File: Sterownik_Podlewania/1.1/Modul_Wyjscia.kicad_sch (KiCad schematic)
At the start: 2 parts, among them J9 Screw_Terminal_01x02, U2 HHG1D-1

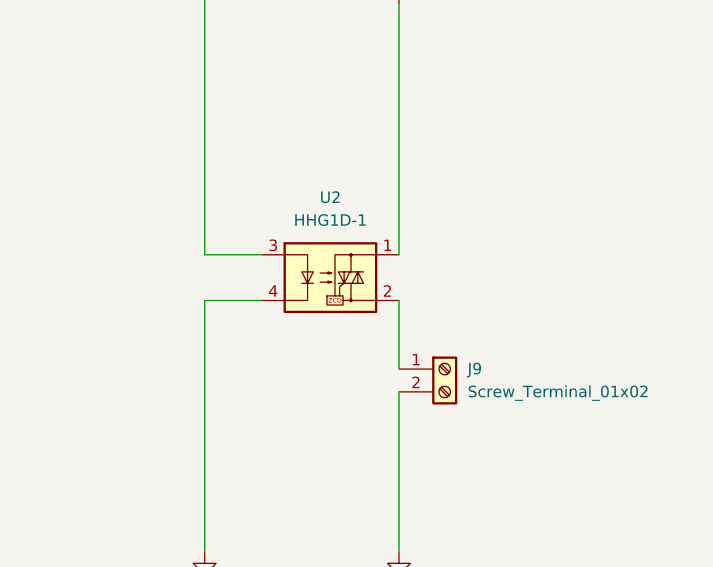
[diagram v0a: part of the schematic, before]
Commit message: Poprawiono błędy połączeń SDA,SCL, dodno drugą magistralę I2C, pociągnięcie nowych ścieżek
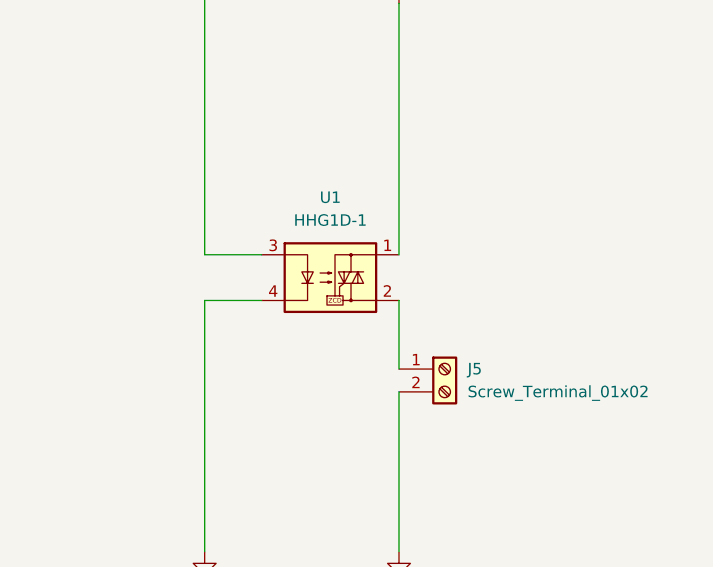
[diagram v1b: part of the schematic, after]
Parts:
- renumbered J9 to J5, U2 to U1
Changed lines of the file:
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@@
 		(dnp no)
 		(fields_autoplaced yes)
-		(property "Reference" "J9"
+		(property "Reference" "J5"
 			(at 127 119.3799 0)
 			(effects
@@
 			(project "Sterownik_Podlewania"
 				(path "/a66bdf1f-0e2a-4cc5-beb1-605f2a3b9885/35770c0e-1214-4968-b3c8-676b712c9d6d"
-					(reference "J10")
+					(reference "J6")
 					(unit 1)
 				)
 				(path "/a66bdf1f-0e2a-4cc5-beb1-605f2a3b9885/6e956094-fc15-4c8c-a9c0-3072cf96750e"
+					(reference "J5")
+					(unit 1)
+				)
+				(path "/a66bdf1f-0e2a-4cc5-beb1-605f2a3b9885/76d9d54a-15a3-400e-aaa0-0af773ab885c"
+					(reference "J8")
+					(unit 1)
+				)
+				(path "/a66bdf1f-0e2a-4cc5-beb1-605f2a3b9885/995f053e-6bfd-4935-9460-d34c9e8248bd"
 					(reference "J9")
 					(unit 1)
 				)
-				(path "/a66bdf1f-0e2a-4cc5-beb1-605f2a3b9885/76d9d54a-15a3-400e-aaa0-0af773ab885c"
-					(reference "J12")
-					(unit 1)
-				)
-				(path "/a66bdf1f-0e2a-4cc5-beb1-605f2a3b9885/995f053e-6bfd-4935-9460-d34c9e8248bd"
-					(reference "J13")
-					(unit 1)
-				)
 				(path "/a66bdf1f-0e2a-4cc5-beb1-605f2a3b9885/aaafd38c-ffc0-4fc7-936b-5b26ec62426f"
-					(reference "J11")
+					(reference "J7")
 					(unit 1)
 				)
@@
 		(dnp no)
 		(fields_autoplaced yes)
-		(property "Reference" "U2"
+		(property "Reference" "U1"
 			(at 111.76 100.33 0)
 			(effects
@@
 			(project ""
 				(path "/a66bdf1f-0e2a-4cc5-beb1-605f2a3b9885/35770c0e-1214-4968-b3c8-676b712c9d6d"
-					(reference "U7")
+					(reference "U2")
 					(unit 1)
 				)
 				(path "/a66bdf1f-0e2a-4cc5-beb1-605f2a3b9885/6e956094-fc15-4c8c-a9c0-3072cf96750e"
-					(reference "U2")
+					(reference "U1")
 					(unit 1)
 				)
 				(path "/a66bdf1f-0e2a-4cc5-beb1-605f2a3b9885/76d9d54a-15a3-400e-aaa0-0af773ab885c"
-					(reference "U9")
+					(reference "U3")
 					(unit 1)
 				)
 				(path "/a66bdf1f-0e2a-4cc5-beb1-605f2a3b9885/995f053e-6bfd-4935-9460-d34c9e8248bd"
-					(reference "U10")
+					(reference "U6")
 					(unit 1)
 				)
 				(path "/a66bdf1f-0e2a-4cc5-beb1-605f2a3b9885/aaafd38c-ffc0-4fc7-936b-5b26ec62426f"
-					(reference "U8")
-					(unit 1)
-				)
+					(reference "U4")
+					(unit 1)
+				)

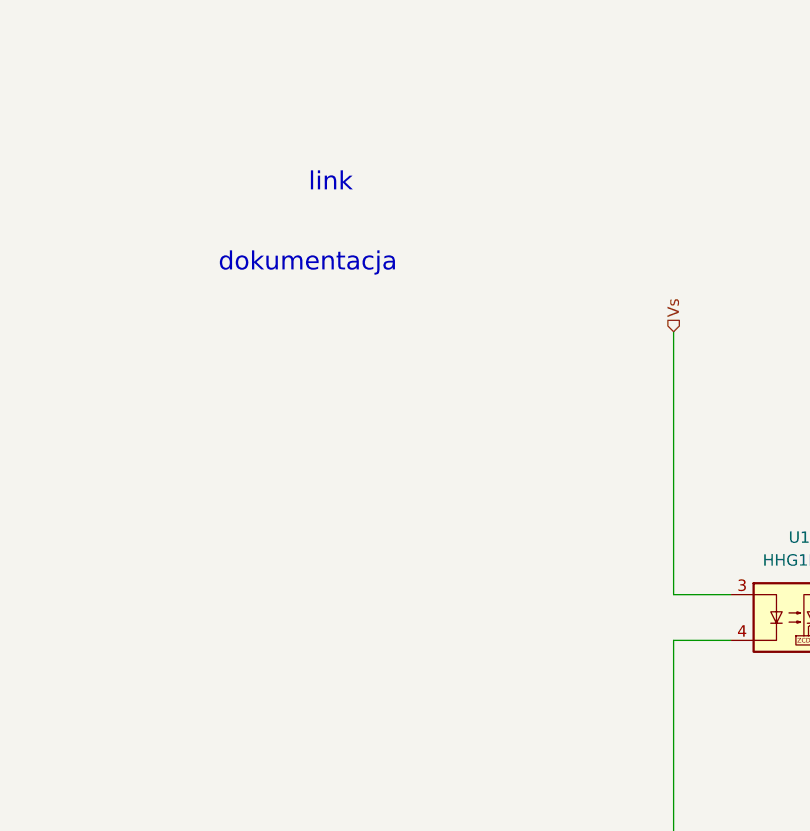
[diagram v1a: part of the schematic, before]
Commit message: Poprawki schematu modułu zaworu, usunięcie przekaźnika, przygotowanie schematu zasilania
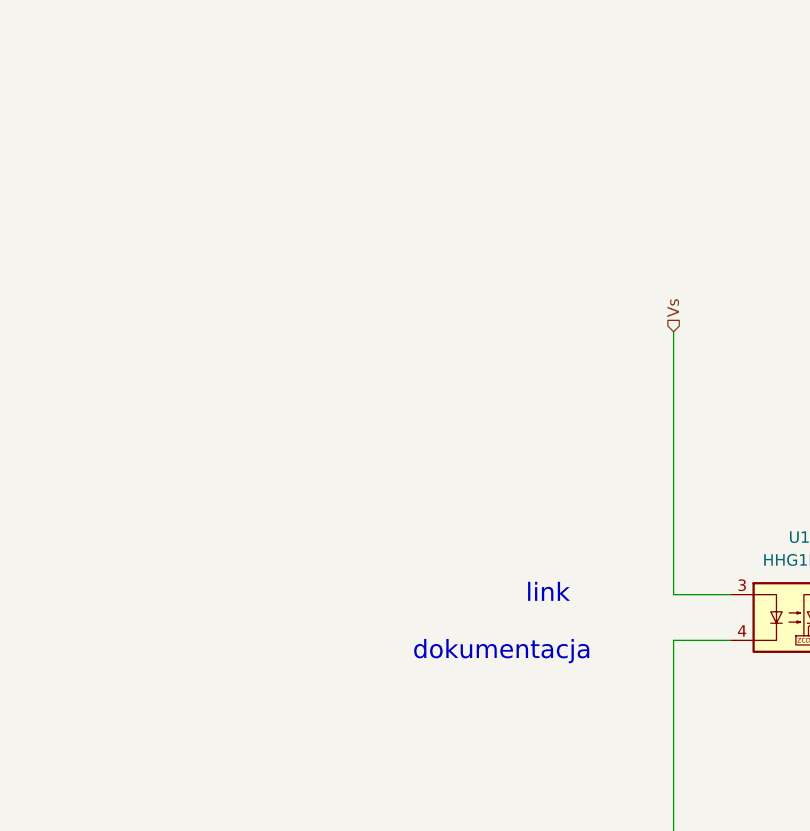
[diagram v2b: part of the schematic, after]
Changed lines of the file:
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@@
 	(text "dokumentacja\n"
 		(exclude_from_sim no)
-		(at 57.15 69.85 0)
+		(at 78.74 113.03 0)
 		(effects
 			(font
@@
 	(text "link"
 		(exclude_from_sim no)
-		(at 59.69 60.96 0)
+		(at 83.82 106.68 0)
 		(effects
 			(font

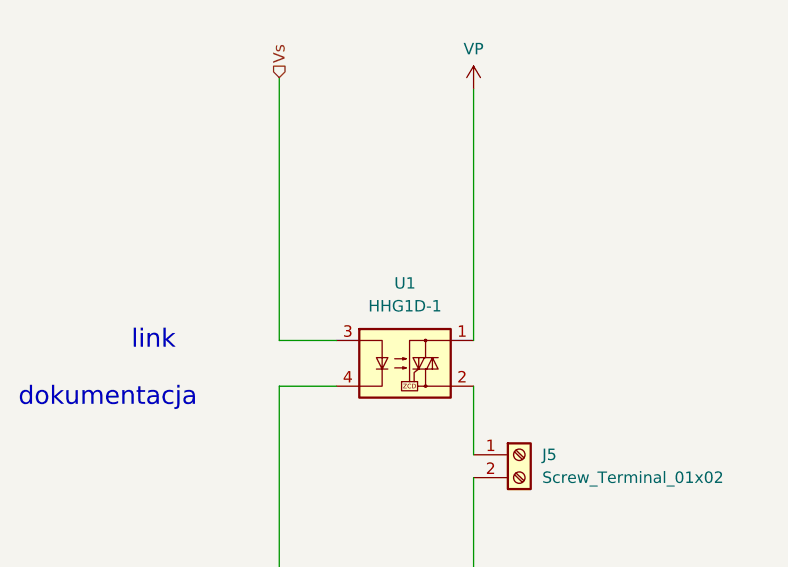
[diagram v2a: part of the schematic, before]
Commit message: Usunięcie zewnętrzego zasilania 12 i stabilizatora napięcia, korekcja zasilania wzmacniacz operacyjny moduł zasilania
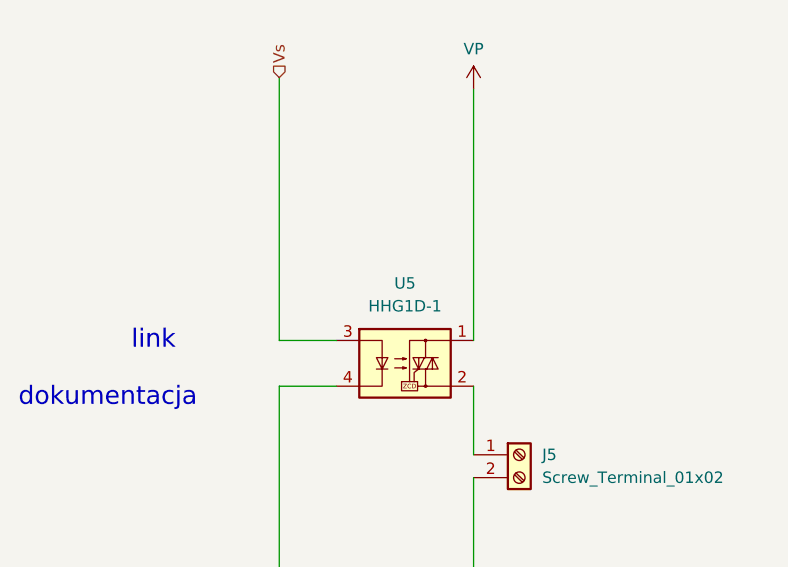
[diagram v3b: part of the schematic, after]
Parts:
- renumbered U1 to U5
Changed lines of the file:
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@@
 		(dnp no)
 		(fields_autoplaced yes)
-		(property "Reference" "#PWR092"
+		(property "Reference" "#PWR047"
 			(at 119.38 146.05 0)
 			(effects
@@
 			(project "Sterownik_Podlewania"
 				(path "/a66bdf1f-0e2a-4cc5-beb1-605f2a3b9885/35770c0e-1214-4968-b3c8-676b712c9d6d"
-					(reference "#PWR093")
+					(reference "#PWR050")
 					(unit 1)
 				)
 				(path "/a66bdf1f-0e2a-4cc5-beb1-605f2a3b9885/6e956094-fc15-4c8c-a9c0-3072cf96750e"
-					(reference "#PWR092")
+					(reference "#PWR047")
 					(unit 1)
 				)
 				(path "/a66bdf1f-0e2a-4cc5-beb1-605f2a3b9885/76d9d54a-15a3-400e-aaa0-0af773ab885c"
-					(reference "#PWR095")
+					(reference "#PWR056")
 					(unit 1)
 				)
 				(path "/a66bdf1f-0e2a-4cc5-beb1-605f2a3b9885/995f053e-6bfd-4935-9460-d34c9e8248bd"
-					(reference "#PWR096")
+					(reference "#PWR059")
 					(unit 1)
 				)
 				(path "/a66bdf1f-0e2a-4cc5-beb1-605f2a3b9885/aaafd38c-ffc0-4fc7-936b-5b26ec62426f"
-					(reference "#PWR094")
+					(reference "#PWR053")
 					(unit 1)
 				)
@@
 		(dnp no)
 		(fields_autoplaced yes)
-		(property "Reference" "#PWR087"
+		(property "Reference" "#PWR046"
 			(at 119.38 82.55 0)
 			(effects
@@
 			(project "Sterownik_Podlewania"
 				(path "/a66bdf1f-0e2a-4cc5-beb1-605f2a3b9885/35770c0e-1214-4968-b3c8-676b712c9d6d"
-					(reference "#PWR088")
+					(reference "#PWR049")
 					(unit 1)
 				)
 				(path "/a66bdf1f-0e2a-4cc5-beb1-605f2a3b9885/6e956094-fc15-4c8c-a9c0-3072cf96750e"
-					(reference "#PWR087")
+					(reference "#PWR046")
 					(unit 1)
 				)
 				(path "/a66bdf1f-0e2a-4cc5-beb1-605f2a3b9885/76d9d54a-15a3-400e-aaa0-0af773ab885c"
-					(reference "#PWR090")
+					(reference "#PWR055")
 					(unit 1)
 				)
 				(path "/a66bdf1f-0e2a-4cc5-beb1-605f2a3b9885/995f053e-6bfd-4935-9460-d34c9e8248bd"
-					(reference "#PWR091")
+					(reference "#PWR058")
 					(unit 1)
 				)
 				(path "/a66bdf1f-0e2a-4cc5-beb1-605f2a3b9885/aaafd38c-ffc0-4fc7-936b-5b26ec62426f"
-					(reference "#PWR089")
+					(reference "#PWR052")
 					(unit 1)
 				)
@@
 		(dnp no)
 		(fields_autoplaced yes)
-		(property "Reference" "#PWR038"
+		(property "Reference" "#PWR045"
 			(at 97.79 146.05 0)
 			(effects
@@
 			(project ""
 				(path "/a66bdf1f-0e2a-4cc5-beb1-605f2a3b9885/35770c0e-1214-4968-b3c8-676b712c9d6d"
-					(reference "#PWR041")
+					(reference "#PWR048")
 					(unit 1)
 				)
 				(path "/a66bdf1f-0e2a-4cc5-beb1-605f2a3b9885/6e956094-fc15-4c8c-a9c0-3072cf96750e"
-					(reference "#PWR038")
+					(reference "#PWR045")
 					(unit 1)
 				)
 				(path "/a66bdf1f-0e2a-4cc5-beb1-605f2a3b9885/76d9d54a-15a3-400e-aaa0-0af773ab885c"
-					(reference "#PWR047")
+					(reference "#PWR054")
 					(unit 1)
 				)
 				(path "/a66bdf1f-0e2a-4cc5-beb1-605f2a3b9885/995f053e-6bfd-4935-9460-d34c9e8248bd"
-					(reference "#PWR048")
+					(reference "#PWR057")
 					(unit 1)
 				)
 				(path "/a66bdf1f-0e2a-4cc5-beb1-605f2a3b9885/aaafd38c-ffc0-4fc7-936b-5b26ec62426f"
-					(reference "#PWR044")
+					(reference "#PWR051")
 					(unit 1)
 				)
@@
 		(dnp no)
 		(fields_autoplaced yes)
-		(property "Reference" "U1"
+		(property "Reference" "U5"
 			(at 111.76 100.33 0)
 			(effects
@@
 			(project ""
 				(path "/a66bdf1f-0e2a-4cc5-beb1-605f2a3b9885/35770c0e-1214-4968-b3c8-676b712c9d6d"
-					(reference "U2")
+					(reference "U6")
 					(unit 1)
 				)
 				(path "/a66bdf1f-0e2a-4cc5-beb1-605f2a3b9885/6e956094-fc15-4c8c-a9c0-3072cf96750e"
-					(reference "U1")
+					(reference "U5")
 					(unit 1)
 				)
 				(path "/a66bdf1f-0e2a-4cc5-beb1-605f2a3b9885/76d9d54a-15a3-400e-aaa0-0af773ab885c"
-					(reference "U3")
+					(reference "U8")
 					(unit 1)
 				)
 				(path "/a66bdf1f-0e2a-4cc5-beb1-605f2a3b9885/995f053e-6bfd-4935-9460-d34c9e8248bd"
-					(reference "U6")
+					(reference "U9")
 					(unit 1)
 				)
 				(path "/a66bdf1f-0e2a-4cc5-beb1-605f2a3b9885/aaafd38c-ffc0-4fc7-936b-5b26ec62426f"
-					(reference "U4")
-					(unit 1)
-				)
+					(reference "U7")
+					(unit 1)
+				)

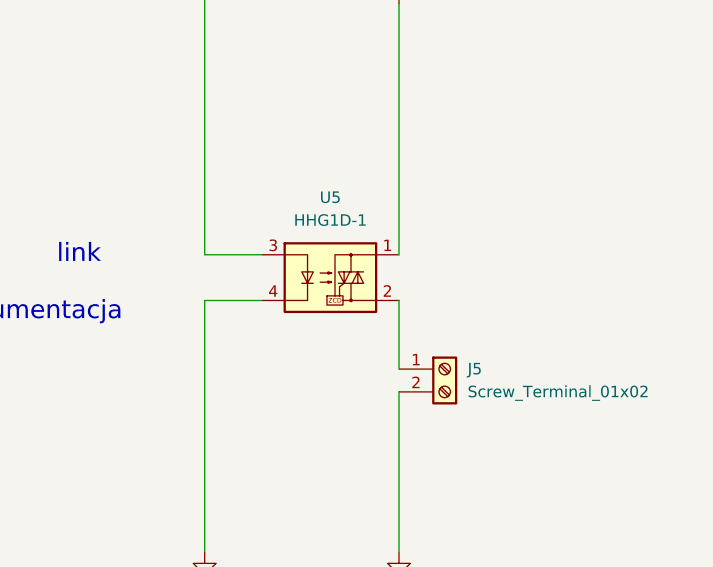
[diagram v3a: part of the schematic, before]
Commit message: Werja plików podesłana Mariuszkowi, dodane opisy i numeracja poprawna dla steronwika, w module poprawniono opis złącze ethernet
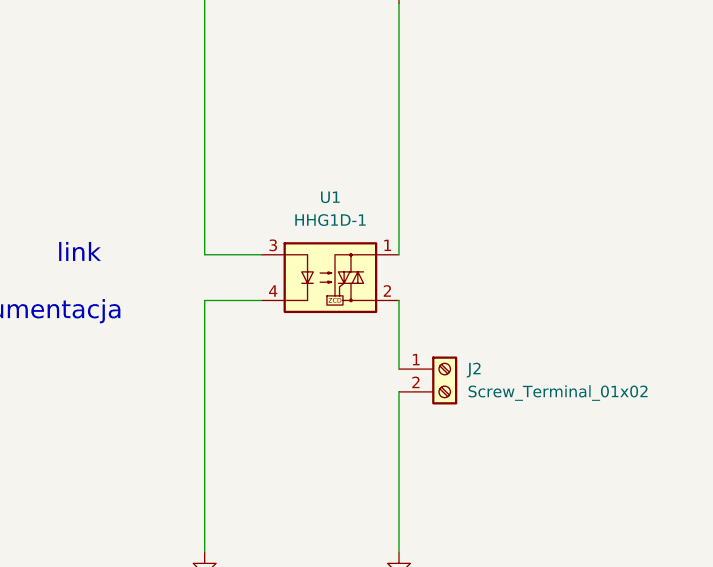
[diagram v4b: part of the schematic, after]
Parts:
- renumbered J5 to J2, U5 to U1
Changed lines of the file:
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@@
 		(dnp no)
 		(fields_autoplaced yes)
-		(property "Reference" "J5"
+		(property "Reference" "J2"
 			(at 127 119.3799 0)
 			(effects
@@
 			(project "Sterownik_Podlewania"
 				(path "/a66bdf1f-0e2a-4cc5-beb1-605f2a3b9885/35770c0e-1214-4968-b3c8-676b712c9d6d"
+					(reference "J3")
+					(unit 1)
+				)
+				(path "/a66bdf1f-0e2a-4cc5-beb1-605f2a3b9885/6e956094-fc15-4c8c-a9c0-3072cf96750e"
+					(reference "J2")
+					(unit 1)
+				)
+				(path "/a66bdf1f-0e2a-4cc5-beb1-605f2a3b9885/76d9d54a-15a3-400e-aaa0-0af773ab885c"
+					(reference "J5")
+					(unit 1)
+				)
+				(path "/a66bdf1f-0e2a-4cc5-beb1-605f2a3b9885/995f053e-6bfd-4935-9460-d34c9e8248bd"
 					(reference "J6")
 					(unit 1)
 				)
-				(path "/a66bdf1f-0e2a-4cc5-beb1-605f2a3b9885/6e956094-fc15-4c8c-a9c0-3072cf96750e"
-					(reference "J5")
-					(unit 1)
-				)
-				(path "/a66bdf1f-0e2a-4cc5-beb1-605f2a3b9885/76d9d54a-15a3-400e-aaa0-0af773ab885c"
-					(reference "J8")
-					(unit 1)
-				)
-				(path "/a66bdf1f-0e2a-4cc5-beb1-605f2a3b9885/995f053e-6bfd-4935-9460-d34c9e8248bd"
-					(reference "J9")
-					(unit 1)
-				)
 				(path "/a66bdf1f-0e2a-4cc5-beb1-605f2a3b9885/aaafd38c-ffc0-4fc7-936b-5b26ec62426f"
-					(reference "J7")
+					(reference "J4")
 					(unit 1)
 				)
@@
 		(dnp no)
 		(fields_autoplaced yes)
-		(property "Reference" "U5"
+		(property "Reference" "U1"
 			(at 111.76 100.33 0)
 			(effects
@@
 			(project ""
 				(path "/a66bdf1f-0e2a-4cc5-beb1-605f2a3b9885/35770c0e-1214-4968-b3c8-676b712c9d6d"
-					(reference "U6")
+					(reference "U2")
 					(unit 1)
 				)
 				(path "/a66bdf1f-0e2a-4cc5-beb1-605f2a3b9885/6e956094-fc15-4c8c-a9c0-3072cf96750e"
+					(reference "U1")
+					(unit 1)
+				)
+				(path "/a66bdf1f-0e2a-4cc5-beb1-605f2a3b9885/76d9d54a-15a3-400e-aaa0-0af773ab885c"
+					(reference "U4")
+					(unit 1)
+				)
+				(path "/a66bdf1f-0e2a-4cc5-beb1-605f2a3b9885/995f053e-6bfd-4935-9460-d34c9e8248bd"
 					(reference "U5")
 					(unit 1)
 				)
-				(path "/a66bdf1f-0e2a-4cc5-beb1-605f2a3b9885/76d9d54a-15a3-400e-aaa0-0af773ab885c"
-					(reference "U8")
-					(unit 1)
-				)
-				(path "/a66bdf1f-0e2a-4cc5-beb1-605f2a3b9885/995f053e-6bfd-4935-9460-d34c9e8248bd"
-					(reference "U9")
-					(unit 1)
-				)
 				(path "/a66bdf1f-0e2a-4cc5-beb1-605f2a3b9885/aaafd38c-ffc0-4fc7-936b-5b26ec62426f"
-					(reference "U7")
-					(unit 1)
-				)
+					(reference "U3")
+					(unit 1)
+				)
